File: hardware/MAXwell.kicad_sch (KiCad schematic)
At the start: 155 parts, among them J1 Conn_02x05_Odd_Even, J2 Conn_02x12_Counter_Clockwise, J3 Barrel_Jack_Switch_Pin3Ring, SW1 SW_Push_Dual, SW10 SW_Wuerth_450301014042, SW11 SW_Wuerth_450301014042, SW12 SW_Wuerth_450301014042, SW13 SW_Wuerth_450301014042, SW2 SW_Push_Dual, SW3 SW_Push_Dual, SW4 SW_Push_Dual, SW5 SW_Wuerth_450301014042, SW6 SW_Push_DPDT, SW7 SW_Wuerth_450301014042, SW8 SW_Wuerth_450301014042, SW9 SW_Wuerth_450301014042, U1 EPM240T100, U2 AMS1117-3.3, U3 D168K, U4 D168K, U5 D168K, U6 D168K, X1 50.000, X2 14.756

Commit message: all footprints assigned
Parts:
- C1: renamed from C11; footprint (none) -> Capacitor_SMD:C_0805_2012Metric_Pad1.18x1.45mm_HandSolder
- C10: renamed from C6; footprint (none) -> Capacitor_SMD:C_0805_2012Metric_Pad1.18x1.45mm_HandSolder
- C11: renamed from C7; footprint (none) -> Capacitor_SMD:C_0805_2012Metric_Pad1.18x1.45mm_HandSolder
- C12: renamed from C8; footprint (none) -> Capacitor_SMD:C_0805_2012Metric_Pad1.18x1.45mm_HandSolder
- C13: footprint (none) -> Capacitor_SMD:C_0805_2012Metric_Pad1.18x1.45mm_HandSolder
- C14: renamed from C15; footprint (none) -> Capacitor_SMD:C_0805_2012Metric_Pad1.18x1.45mm_HandSolder
- C15: renamed from C20; footprint (none) -> Capacitor_SMD:C_0805_2012Metric_Pad1.18x1.45mm_HandSolder
- C16: renamed from C25; footprint (none) -> Capacitor_SMD:C_0805_2012Metric_Pad1.18x1.45mm_HandSolder
- C17: renamed from C23; footprint (none) -> Capacitor_SMD:C_0805_2012Metric_Pad1.18x1.45mm_HandSolder
- C18: renamed from C19; footprint (none) -> Capacitor_SMD:C_0805_2012Metric_Pad1.18x1.45mm_HandSolder
- C19: renamed from C17; footprint (none) -> Capacitor_THT:CP_Radial_D5.0mm_P2.00mm; Part-Nr (none) -> M-A 100U 16-2
- C2: renamed from C12; footprint (none) -> Capacitor_SMD:C_0805_2012Metric_Pad1.18x1.45mm_HandSolder
- C20: renamed from C24; footprint (none) -> Capacitor_SMD:C_0805_2012Metric_Pad1.18x1.45mm_HandSolder
- C21: renamed from C22; footprint (none) -> Capacitor_SMD:C_0805_2012Metric_Pad1.18x1.45mm_HandSolder
- C22: renamed from C18; footprint (none) -> Capacitor_SMD:C_0805_2012Metric_Pad1.18x1.45mm_HandSolder
- C23: renamed from C21; footprint (none) -> Capacitor_SMD:C_0805_2012Metric_Pad1.18x1.45mm_HandSolder
- C24: renamed from C9; footprint (none) -> Capacitor_SMD:C_0805_2012Metric_Pad1.18x1.45mm_HandSolder
- C25: renamed from C10; footprint (none) -> Capacitor_SMD:C_0805_2012Metric_Pad1.18x1.45mm_HandSolder
- C3: renamed from C16; footprint (none) -> Capacitor_SMD:C_0805_2012Metric_Pad1.18x1.45mm_HandSolder
- C4: renamed from C1; footprint (none) -> Capacitor_SMD:C_0805_2012Metric_Pad1.18x1.45mm_HandSolder
- C5: renamed from C2; footprint (none) -> Capacitor_SMD:C_0805_2012Metric_Pad1.18x1.45mm_HandSolder
- C6: renamed from C3; footprint (none) -> Capacitor_SMD:C_0805_2012Metric_Pad1.18x1.45mm_HandSolder
- C7: renamed from C4; footprint (none) -> Capacitor_SMD:C_0805_2012Metric_Pad1.18x1.45mm_HandSolder
- C8: renamed from C5; footprint (none) -> Capacitor_SMD:C_0805_2012Metric_Pad1.18x1.45mm_HandSolder
- C9: renamed from C14; footprint (none) -> Capacitor_SMD:C_0805_2012Metric_Pad1.18x1.45mm_HandSolder
- D1: renamed from D5; footprint (none) -> LED_SMD:LED_0805_2012Metric_Pad1.15x1.40mm_HandSolder
- D10: renamed from D13; footprint (none) -> LED_SMD:LED_0805_2012Metric_Pad1.15x1.40mm_HandSolder
- D11: renamed from D14; footprint (none) -> LED_SMD:LED_0805_2012Metric_Pad1.15x1.40mm_HandSolder
- D12: renamed from D15; footprint (none) -> LED_SMD:LED_0805_2012Metric_Pad1.15x1.40mm_HandSolder
- D13: renamed from D16; footprint (none) -> LED_SMD:LED_0805_2012Metric_Pad1.15x1.40mm_HandSolder
- D14: renamed from D1; footprint (none) -> LED_SMD:LED_0805_2012Metric_Pad1.15x1.40mm_HandSolder
- D15: renamed from D2; footprint (none) -> LED_SMD:LED_0805_2012Metric_Pad1.15x1.40mm_HandSolder
- D16: renamed from D4; footprint (none) -> LED_SMD:LED_0805_2012Metric_Pad1.15x1.40mm_HandSolder
- D17: footprint (none) -> LED_SMD:LED_0805_2012Metric_Pad1.15x1.40mm_HandSolder
- D2: renamed from D6; footprint (none) -> LED_SMD:LED_0805_2012Metric_Pad1.15x1.40mm_HandSolder
- D3: renamed from D7; footprint (none) -> LED_SMD:LED_0805_2012Metric_Pad1.15x1.40mm_HandSolder
- D4: renamed from D8; footprint (none) -> LED_SMD:LED_0805_2012Metric_Pad1.15x1.40mm_HandSolder
- D5: renamed from D3; footprint (none) -> LED_SMD:LED_0805_2012Metric_Pad1.15x1.40mm_HandSolder
- D6: renamed from D9; footprint (none) -> LED_SMD:LED_0805_2012Metric_Pad1.15x1.40mm_HandSolder
- D7: renamed from D10; footprint (none) -> LED_SMD:LED_0805_2012Metric_Pad1.15x1.40mm_HandSolder
- D8: renamed from D11; footprint (none) -> LED_SMD:LED_0805_2012Metric_Pad1.15x1.40mm_HandSolder
- D9: renamed from D12; footprint (none) -> LED_SMD:LED_0805_2012Metric_Pad1.15x1.40mm_HandSolder
- J2: footprint (none) -> Connector_PinHeader_2.54mm:PinHeader_2x12_P2.54mm_Horizontal
- J3: footprint Connector_BarrelJack:BarrelJack_CUI_PJ-063AH_Horizontal_CircularHoles -> Connector_BarrelJack:BarrelJack_Horizontal
- R1: renamed from R5; footprint (none) -> Resistor_SMD:R_0805_2012Metric_Pad1.20x1.40mm_HandSolder
- R10: renamed from R37; footprint (none) -> Resistor_SMD:R_0805_2012Metric_Pad1.20x1.40mm_HandSolder
- R11: renamed from R38; footprint (none) -> Resistor_SMD:R_0805_2012Metric_Pad1.20x1.40mm_HandSolder
- R12: renamed from R39; footprint (none) -> Resistor_SMD:R_0805_2012Metric_Pad1.20x1.40mm_HandSolder
- R13: renamed from R40; footprint (none) -> Resistor_SMD:R_0805_2012Metric_Pad1.20x1.40mm_HandSolder
- R14: renamed from R25; footprint (none) -> Resistor_SMD:R_0805_2012Metric_Pad1.20x1.40mm_HandSolder
- R15: renamed from R26; footprint (none) -> Resistor_SMD:R_0805_2012Metric_Pad1.20x1.40mm_HandSolder
- R16: renamed from R27; footprint (none) -> Resistor_SMD:R_0805_2012Metric_Pad1.20x1.40mm_HandSolder
- R17: renamed from R28; footprint (none) -> Resistor_SMD:R_0805_2012Metric_Pad1.20x1.40mm_HandSolder
- R18: renamed from R29; footprint (none) -> Resistor_SMD:R_0805_2012Metric_Pad1.20x1.40mm_HandSolder
- R19: renamed from R30; footprint (none) -> Resistor_SMD:R_0805_2012Metric_Pad1.20x1.40mm_HandSolder
- R2: renamed from R6; footprint (none) -> Resistor_SMD:R_0805_2012Metric_Pad1.20x1.40mm_HandSolder
- R20: renamed from R31; footprint (none) -> Resistor_SMD:R_0805_2012Metric_Pad1.20x1.40mm_HandSolder
- R21: renamed from R32; footprint (none) -> Resistor_SMD:R_0805_2012Metric_Pad1.20x1.40mm_HandSolder
- R22: renamed from R41; footprint (none) -> Resistor_SMD:R_0805_2012Metric_Pad1.20x1.40mm_HandSolder
- R23: renamed from R42; footprint (none) -> Resistor_SMD:R_0805_2012Metric_Pad1.20x1.40mm_HandSolder
- R24: renamed from R43; footprint (none) -> Resistor_SMD:R_0805_2012Metric_Pad1.20x1.40mm_HandSolder
- R25: renamed from R44; footprint (none) -> Resistor_SMD:R_0805_2012Metric_Pad1.20x1.40mm_HandSolder
- R26: renamed from R45; footprint (none) -> Resistor_SMD:R_0805_2012Metric_Pad1.20x1.40mm_HandSolder
- R27: renamed from R46; footprint (none) -> Resistor_SMD:R_0805_2012Metric_Pad1.20x1.40mm_HandSolder
- R28: renamed from R47; footprint (none) -> Resistor_SMD:R_0805_2012Metric_Pad1.20x1.40mm_HandSolder
- R29: renamed from R48; footprint (none) -> Resistor_SMD:R_0805_2012Metric_Pad1.20x1.40mm_HandSolder
- R3: renamed from R7; footprint (none) -> Resistor_SMD:R_0805_2012Metric_Pad1.20x1.40mm_HandSolder
- R30: renamed from R64; footprint (none) -> Resistor_SMD:R_0805_2012Metric_Pad1.20x1.40mm_HandSolder
- R31: renamed from R63; footprint (none) -> Resistor_SMD:R_0805_2012Metric_Pad1.20x1.40mm_HandSolder
- R32: renamed from R62; footprint (none) -> Resistor_SMD:R_0805_2012Metric_Pad1.20x1.40mm_HandSolder
- R33: renamed from R61; footprint (none) -> Resistor_SMD:R_0805_2012Metric_Pad1.20x1.40mm_HandSolder
- R34: renamed from R17; footprint (none) -> Resistor_SMD:R_0805_2012Metric_Pad1.20x1.40mm_HandSolder
- R35: renamed from R18; footprint (none) -> Resistor_SMD:R_0805_2012Metric_Pad1.20x1.40mm_HandSolder
- R36: renamed from R19; footprint (none) -> Resistor_SMD:R_0805_2012Metric_Pad1.20x1.40mm_HandSolder
- R37: renamed from R20; footprint (none) -> Resistor_SMD:R_0805_2012Metric_Pad1.20x1.40mm_HandSolder
- R38: renamed from R21; footprint (none) -> Resistor_SMD:R_0805_2012Metric_Pad1.20x1.40mm_HandSolder
- R39: renamed from R22; footprint (none) -> Resistor_SMD:R_0805_2012Metric_Pad1.20x1.40mm_HandSolder
- R4: renamed from R8; footprint (none) -> Resistor_SMD:R_0805_2012Metric_Pad1.20x1.40mm_HandSolder
- R40: renamed from R23; footprint (none) -> Resistor_SMD:R_0805_2012Metric_Pad1.20x1.40mm_HandSolder
- R41: renamed from R24; footprint (none) -> Resistor_SMD:R_0805_2012Metric_Pad1.20x1.40mm_HandSolder
- R42: renamed from R58; footprint (none) -> Resistor_SMD:R_0805_2012Metric_Pad1.20x1.40mm_HandSolder
- R43: renamed from R59; footprint (none) -> Resistor_SMD:R_0805_2012Metric_Pad1.20x1.40mm_HandSolder
- R44: renamed from R60; footprint (none) -> Resistor_SMD:R_0805_2012Metric_Pad1.20x1.40mm_HandSolder
- R45: renamed from R52; footprint (none) -> Resistor_SMD:R_0805_2012Metric_Pad1.20x1.40mm_HandSolder
- R46: renamed from R53; footprint (none) -> Resistor_SMD:R_0805_2012Metric_Pad1.20x1.40mm_HandSolder
- R47: renamed from R54; footprint (none) -> Resistor_SMD:R_0805_2012Metric_Pad1.20x1.40mm_HandSolder
- R48: renamed from R49; footprint (none) -> Resistor_SMD:R_0805_2012Metric_Pad1.20x1.40mm_HandSolder
- R49: renamed from R50; footprint (none) -> Resistor_SMD:R_0805_2012Metric_Pad1.20x1.40mm_HandSolder
- R5: renamed from R3; footprint (none) -> Resistor_SMD:R_0805_2012Metric_Pad1.20x1.40mm_HandSolder
- R50: renamed from R55; footprint (none) -> Resistor_SMD:R_0805_2012Metric_Pad1.20x1.40mm_HandSolder
- R51: renamed from R56; footprint (none) -> Resistor_SMD:R_0805_2012Metric_Pad1.20x1.40mm_HandSolder
- R52: renamed from R9; footprint (none) -> Resistor_SMD:R_0805_2012Metric_Pad1.20x1.40mm_HandSolder
- R53: renamed from R10; footprint (none) -> Resistor_SMD:R_0805_2012Metric_Pad1.20x1.40mm_HandSolder
- R54: renamed from R11; footprint (none) -> Resistor_SMD:R_0805_2012Metric_Pad1.20x1.40mm_HandSolder
- R55: renamed from R12; footprint (none) -> Resistor_SMD:R_0805_2012Metric_Pad1.20x1.40mm_HandSolder
- R56: renamed from R13; footprint (none) -> Resistor_SMD:R_0805_2012Metric_Pad1.20x1.40mm_HandSolder
- R57: renamed from R14; footprint (none) -> Resistor_SMD:R_0805_2012Metric_Pad1.20x1.40mm_HandSolder
- R58: renamed from R15; footprint (none) -> Resistor_SMD:R_0805_2012Metric_Pad1.20x1.40mm_HandSolder
- R59: renamed from R16; footprint (none) -> Resistor_SMD:R_0805_2012Metric_Pad1.20x1.40mm_HandSolder
- R6: renamed from R33; footprint (none) -> Resistor_SMD:R_0805_2012Metric_Pad1.20x1.40mm_HandSolder
- R60: renamed from R51; footprint (none) -> Resistor_SMD:R_0805_2012Metric_Pad1.20x1.40mm_HandSolder
- R61: renamed from R57; footprint (none) -> Resistor_SMD:R_0805_2012Metric_Pad1.20x1.40mm_HandSolder
- R62: renamed from R1; footprint (none) -> Resistor_SMD:R_0805_2012Metric_Pad1.20x1.40mm_HandSolder
- R63: renamed from R2; footprint (none) -> Resistor_SMD:R_0805_2012Metric_Pad1.20x1.40mm_HandSolder
- R64: renamed from R72; footprint (none) -> Resistor_SMD:R_0805_2012Metric_Pad1.20x1.40mm_HandSolder
- R65: renamed from R4; footprint (none) -> Resistor_SMD:R_0805_2012Metric_Pad1.20x1.40mm_HandSolder
- R66: renamed from R73; footprint (none) -> Resistor_SMD:R_0805_2012Metric_Pad1.20x1.40mm_HandSolder
- R67: renamed from R74; footprint (none) -> Resistor_SMD:R_0805_2012Metric_Pad1.20x1.40mm_HandSolder
- R68: renamed from R87; footprint (none) -> Resistor_SMD:R_0805_2012Metric_Pad1.20x1.40mm_HandSolder
- R69: renamed from R81; footprint (none) -> Resistor_SMD:R_0805_2012Metric_Pad1.20x1.40mm_HandSolder
- R7: renamed from R34; footprint (none) -> Resistor_SMD:R_0805_2012Metric_Pad1.20x1.40mm_HandSolder
- R70: renamed from R69; footprint (none) -> Resistor_SMD:R_0805_2012Metric_Pad1.20x1.40mm_HandSolder
- R71: renamed from R88; footprint (none) -> Resistor_SMD:R_0805_2012Metric_Pad1.20x1.40mm_HandSolder
- R72: renamed from R89; footprint (none) -> Resistor_SMD:R_0805_2012Metric_Pad1.20x1.40mm_HandSolder
- R73: renamed from R82; footprint (none) -> Resistor_SMD:R_0805_2012Metric_Pad1.20x1.40mm_HandSolder
- R74: renamed from R83; footprint (none) -> Resistor_SMD:R_0805_2012Metric_Pad1.20x1.40mm_HandSolder
- R75: renamed from R70; footprint (none) -> Resistor_SMD:R_0805_2012Metric_Pad1.20x1.40mm_HandSolder
- R76: renamed from R71; footprint (none) -> Resistor_SMD:R_0805_2012Metric_Pad1.20x1.40mm_HandSolder
- R77: renamed from R65; footprint (none) -> Resistor_SMD:R_0805_2012Metric_Pad1.20x1.40mm_HandSolder
- R78: renamed from R84; footprint (none) -> Resistor_SMD:R_0805_2012Metric_Pad1.20x1.40mm_HandSolder
- R79: renamed from R78; footprint (none) -> Resistor_SMD:R_0805_2012Metric_Pad1.20x1.40mm_HandSolder
- R8: renamed from R35; footprint (none) -> Resistor_SMD:R_0805_2012Metric_Pad1.20x1.40mm_HandSolder
- R80: renamed from R68; footprint (none) -> Resistor_SMD:R_0805_2012Metric_Pad1.20x1.40mm_HandSolder
- R81: renamed from R75; footprint (none) -> Resistor_SMD:R_0805_2012Metric_Pad1.20x1.40mm_HandSolder
- R82: renamed from R85; footprint (none) -> Resistor_SMD:R_0805_2012Metric_Pad1.20x1.40mm_HandSolder
- R83: renamed from R86; footprint (none) -> Resistor_SMD:R_0805_2012Metric_Pad1.20x1.40mm_HandSolder
- R84: renamed from R79; footprint (none) -> Resistor_SMD:R_0805_2012Metric_Pad1.20x1.40mm_HandSolder
- R85: renamed from R80; footprint (none) -> Resistor_SMD:R_0805_2012Metric_Pad1.20x1.40mm_HandSolder
- R86: renamed from R67; footprint (none) -> Resistor_SMD:R_0805_2012Metric_Pad1.20x1.40mm_HandSolder
- R87: renamed from R66; footprint (none) -> Resistor_SMD:R_0805_2012Metric_Pad1.20x1.40mm_HandSolder
- R88: renamed from R76; footprint (none) -> Resistor_SMD:R_0805_2012Metric_Pad1.20x1.40mm_HandSolder
- R89: renamed from R77; footprint (none) -> Resistor_SMD:R_0805_2012Metric_Pad1.20x1.40mm_HandSolder
- R9: renamed from R36; footprint (none) -> Resistor_SMD:R_0805_2012Metric_Pad1.20x1.40mm_HandSolder
- SW10: renamed from SW12; footprint Button_Switch_THT:SW_Slide-03_Wuerth-WS-SLTV_10x2.5x6.4_P2.54mm -> Library:SW_Slide_SPDT_Straight_12.8mm_6.9mm
- SW11: renamed from SW10; footprint Button_Switch_THT:SW_Slide-03_Wuerth-WS-SLTV_10x2.5x6.4_P2.54mm -> Library:SW_Slide_SPDT_Straight_12.8mm_6.9mm
- SW12: renamed from SW5; footprint Button_Switch_THT:SW_Slide-03_Wuerth-WS-SLTV_10x2.5x6.4_P2.54mm -> Library:SW_Slide_SPDT_Straight_12.8mm_6.9mm
- SW13: renamed from SW9; footprint Button_Switch_THT:SW_Slide-03_Wuerth-WS-SLTV_10x2.5x6.4_P2.54mm -> Library:SW_Slide_SPDT_Straight_12.8mm_6.9mm
- SW5: renamed from SW8; footprint Button_Switch_THT:SW_Slide-03_Wuerth-WS-SLTV_10x2.5x6.4_P2.54mm -> Library:SW_Slide_SPDT_Straight_12.8mm_6.9mm
- SW6: renamed from SW13; footprint Button_Switch_THT:SW_Slide-03_Wuerth-WS-SLTV_10x2.5x6.4_P2.54mm -> Library:SW_Slide_SPDT_Straight_12.8mm_6.9mm
- SW7: renamed from SW11; footprint Button_Switch_THT:SW_Slide-03_Wuerth-WS-SLTV_10x2.5x6.4_P2.54mm -> Library:SW_Slide_SPDT_Straight_12.8mm_6.9mm
- SW8: renamed from SW7; footprint Button_Switch_THT:SW_Slide-03_Wuerth-WS-SLTV_10x2.5x6.4_P2.54mm -> Library:SW_Slide_SPDT_Straight_12.8mm_6.9mm
- SW9: renamed from SW6; footprint (none) -> Button_Switch_THT:SW_Push_2P2T_Toggle_CK_PVA2OAH5xxxxxxV2
- U1: renamed from U5; Part-Nr SA 56-11 RT Alternative: SC 39-11 GN -> SA 56-11 RT
- renumbered SW4 to SW1, SW1 to SW3, SW3 to SW4, U4 to U2, U6 to U3, U3 to U4, U1 to U5, U2 to U6
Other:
- note added: "TODO: Prüfen, ob Prog. Header richtig angeschlossen Pin 10 mit GND Verbidung richtig?"
- note removed: "TODO: Prüfen, ob Prog. Header richtig angeschlossen"

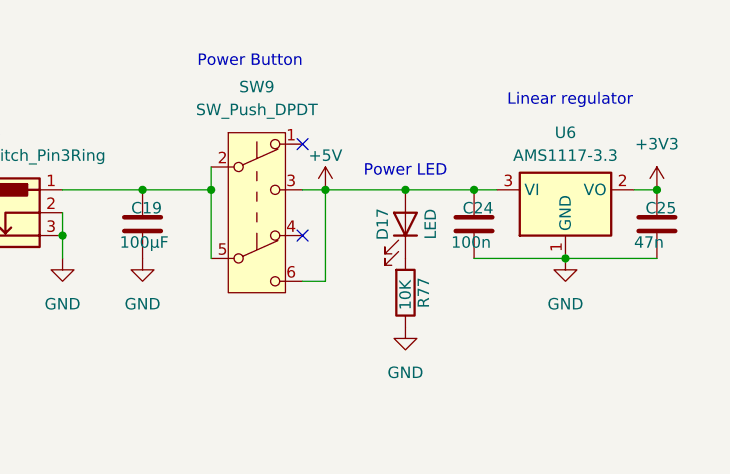
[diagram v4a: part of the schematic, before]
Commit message: ERC applied and fixed missing power flags
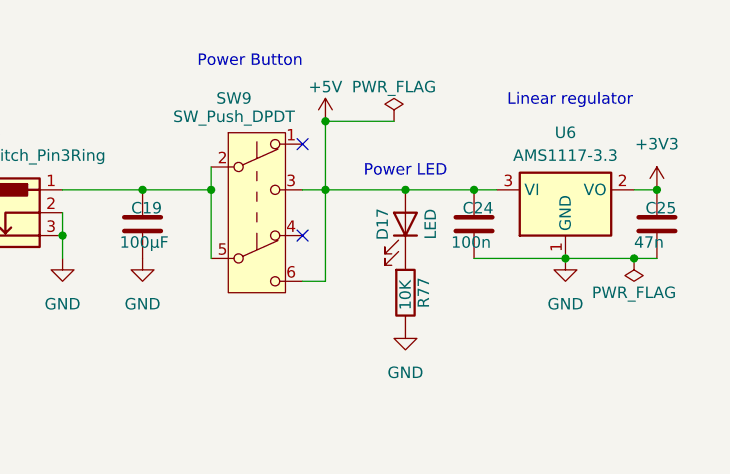
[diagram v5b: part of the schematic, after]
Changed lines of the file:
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@@
 	)
 	(junction
+		(at 274.32 39.37)
+		(diameter 0)
+		(color 0 0 0 0)
+	)
+	(junction
 		(at 31.75 34.29)
 		(diameter 0)
@@
 	)
 	(junction
+		(at 240.03 24.13)
+		(diameter 0)
+		(color 0 0 0 0)
+	)
+	(junction
 		(at 64.77 111.76)
 		(diameter 0)
@@
 	(wire
 		(pts
+			(xy 274.32 39.37) (xy 276.86 39.37)
+		)
+		(stroke
+			(width 0)
+			(type default)
+		)
+	)
+	(wire
+		(pts
 			(xy 181.61 29.21) (xy 181.61 35.56)
 		)
@@
 	(wire
 		(pts
+			(xy 247.65 24.13) (xy 240.03 24.13)
+		)
+		(stroke
+			(width 0)
+			(type default)
+		)
+	)
+	(wire
+		(pts
 			(xy 142.24 83.82) (xy 146.05 83.82)
 		)
@@
 	(wire
 		(pts
+			(xy 240.03 24.13) (xy 240.03 31.75)
+		)
+		(stroke
+			(width 0)
+			(type default)
+		)
+	)
+	(wire
+		(pts
 			(xy 60.96 116.84) (xy 91.44 116.84)
 		)
@@
 	(wire
 		(pts
-			(xy 266.7 39.37) (xy 276.86 39.37)
+			(xy 266.7 39.37) (xy 274.32 39.37)
 		)
 		(stroke
@@
 	(symbol
 		(lib_id "power:+5V")
-		(at 240.03 31.75 0)
+		(at 240.03 24.13 0)
 		(unit 1)
 		(exclude_from_sim no)
@@
 		(dnp no)
 		(property "Reference" "#PWR043"
-			(at 240.03 35.56 0)
+			(at 240.03 27.94 0)
 			(effects
 				(font
@@
 		)
 		(property "Value" "+5V"
-			(at 240.03 27.94 0)
+			(at 240.03 20.32 0)
 			(effects
 				(font
@@
 		)
 		(property "Footprint" ""
-			(at 240.03 31.75 0)
+			(at 240.03 24.13 0)
 			(effects
 				(font
@@
 		)
 		(property "Datasheet" ""
-			(at 240.03 31.75 0)
+			(at 240.03 24.13 0)
 			(effects
 				(font
@@
 		)
 		(property "Description" "Power symbol creates a global label with name \"+5V\""
-			(at 240.03 31.75 0)
+			(at 240.03 24.13 0)
 			(effects
 				(font
@@
 		(on_board yes)
 		(dnp no)
-		(fields_autoplaced yes)
 		(property "Reference" "SW9"
-			(at 232.41 20.32 0)
+			(at 229.87 21.59 0)
 			(effects
 				(font
@@
 		)
 		(property "Value" "SW_Push_DPDT"
-			(at 232.41 22.86 0)
+			(at 229.87 23.622 0)
 			(effects
 				(font
@@
 	)
 	(symbol
+		(lib_id "power:PWR_FLAG")
+		(at 274.32 39.37 180)
+		(unit 1)
+		(exclude_from_sim no)
+		(in_bom yes)
+		(on_board yes)
+		(dnp no)
+		(property "Reference" "#FLG02"
+			(at 274.32 41.275 0)
+			(effects
+				(font
+					(size 1.27 1.27)
+				)
+				(hide yes)
+			)
+		)
+		(property "Value" "PWR_FLAG"
+			(at 274.32 43.18 0)
+			(effects
+				(font
+					(size 1.27 1.27)
+				)
+			)
+		)
+		(property "Footprint" ""
+			(at 274.32 39.37 0)
+			(effects
+				(font
+					(size 1.27 1.27)
+				)
+				(hide yes)
+			)
+		)
+		(property "Datasheet" "~"
+			(at 274.32 39.37 0)
+			(effects
+				(font
+					(size 1.27 1.27)
+				)
+				(hide yes)
+			)
+		)
+		(property "Description" "Special symbol for telling ERC where power comes from"
+			(at 274.32 39.37 0)
+			(effects
+				(font
+					(size 1.27 1.27)
+				)
+				(hide yes)
+			)
+		)
+		(pin "1"
+		)
+		(instances
+			(project "MAXwell"
+				(path "/fb6af602-47f1-4d32-af46-a424ef1eeea7"
+					(reference "#FLG02")
+					(unit 1)
+				)
+			)
+		)
+	)
+	(symbol
 		(lib_id "power:+3V3")
 		(at 31.75 19.05 0)
@@
 					(unit 1)
 				)
+			)
+		)
+	)
+	(symbol
+		(lib_id "power:PWR_FLAG")
+		(at 247.65 24.13 0)
+		(unit 1)
+		(exclude_from_sim no)
+		(in_bom yes)
+		(on_board yes)
+		(dnp no)
+		(property "Reference" "#FLG01"
+			(at 247.65 22.225 0)
+			(effects
+				(font
+					(size 1.27 1.27)
+				)
+				(hide yes)
+			)
+		)
+		(property "Value" "PWR_FLAG"
+			(at 247.65 20.32 0)
+			(effects
+				(font
+					(size 1.27 1.27)
+				)
+			)
+		)
+		(property "Footprint" ""
+			(at 247.65 24.13 0)
+			(effects
+				(font
+					(size 1.27 1.27)
+				)
+				(hide yes)
+			)
+		)
+		(property "Datasheet" "~"
+			(at 247.65 24.13 0)
+			(effects
+				(font
+					(size 1.27 1.27)
+				)
+				(hide yes)
+			)
+		)
+		(property "Description" "Special symbol for telling ERC where power comes from"
+			(at 247.65 24.13 0)
+			(effects
+				(font
+					(size 1.27 1.27)
+				)
+				(hide yes)
+			)
+		)
+		(pin "1"
+		)
+		(instances
+			(project "MAXwell"
+				(path "/fb6af602-47f1-4d32-af46-a424ef1eeea7"
+					(reference "#FLG01")
+					(unit 1)
+				)

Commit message: started routing
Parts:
- J2: symbol Connector_Generic:Conn_02x12_Counter_Clockwise -> Connector_Generic:Conn_02x12_Odd_Even
- SW1, SW2, SW3, SW4: footprint Button_Switch_THT:SW_PUSH-12mm -> Library:SW_PUSH-12mm
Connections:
- net +3V3: now also J2.3 (Pin_3); no longer J2.2 (Pin_2)
- net GND: now also J2.2 (Pin_2), J2.4 (Pin_4), J2.6 (Pin_6), J2.8 (Pin_8); no longer J2.21 (Pin_21), J2.22 (Pin_22), J2.23 (Pin_23), J2.24 (Pin_24)
- net at U5.62 (IO2_62/GCLK2): now also J2.5 (Pin_5); no longer J2.3 (Pin_3)
- net at U5.64 (IO2_64/GCLK3): now also J2.7 (Pin_7); no longer J2.4 (Pin_4)
- net at U5.66 (IO2_66): now also J2.9 (Pin_9); no longer J2.5 (Pin_5)
- net at U5.67 (IO2_67): now also J2.11 (Pin_11); no longer J2.6 (Pin_6)
- net at U5.68 (IO2_68): now also J2.13 (Pin_13); no longer J2.7 (Pin_7)
- net at U5.69 (IO2_69): now also J2.15 (Pin_15); no longer J2.8 (Pin_8)
- net at U5.70 (IO2_70): now also J2.17 (Pin_17); no longer J2.9 (Pin_9)
- net at U5.71 (IO2_71): now also J2.19 (Pin_19); no longer J2.10 (Pin_10)
- net at U5.72 (IO2_72): now also J2.21 (Pin_21); no longer J2.11 (Pin_11)
- net at U5.73 (IO2_73): now also J2.23 (Pin_23); no longer J2.12 (Pin_12)
- net at U5.74 (IO2_74): now also J2.24 (Pin_24); no longer J2.13 (Pin_13)
- net at U5.75 (IO2_75): now also J2.22 (Pin_22); no longer J2.14 (Pin_14)
- net at U5.76 (IO2_76): now also J2.20 (Pin_20); no longer J2.15 (Pin_15)
- net at U5.77 (IO2_77): now also J2.18 (Pin_18); no longer J2.16 (Pin_16)
- net at U5.78 (IO2_78): now also J2.16 (Pin_16); no longer J2.17 (Pin_17)
- net at U5.81 (IO2_81): now also J2.14 (Pin_14); no longer J2.18 (Pin_18)
- net at U5.82 (IO2_82): now also J2.12 (Pin_12); no longer J2.19 (Pin_19)
- net at U5.83 (IO2_83): now also J2.10 (Pin_10); no longer J2.20 (Pin_20)
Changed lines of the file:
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@@
 	)
 	(symbol
-		(lib_id "Connector_Generic:Conn_02x12_Counter_Clockwise")
+		(lib_id "Connector_Generic:Conn_02x12_Odd_Even")
 		(at 171.45 91.44 270)
 		(unit 1)
@@
 			)
 		)
-		(property "Description" "Generic connector, double row, 02x12, counter clockwise pin numbering scheme (similar to DIP package numbering), script generated (kicad-library-utils/schlib/autogen/connector/)"
+		(property "Description" "Generic connector, double row, 02x12, odd/even pin numbering scheme (row 1 odd numbers, row 2 even numbers), script generated (kicad-library-utils/schlib/autogen/connector/)"
 			(at 171.45 91.44 0)
 			(effects
@@
 			)
 		)
-		(property "Footprint" "Button_Switch_THT:SW_PUSH-12mm"
+		(property "Footprint" "Library:SW_PUSH-12mm"
 			(at 163.83 177.8 0)
 			(effects
@@
 			)
 		)
-		(property "Footprint" "Button_Switch_THT:SW_PUSH-12mm"
+		(property "Footprint" "Library:SW_PUSH-12mm"
 			(at 101.6 177.8 0)
 			(effects
@@
 			)
 		)
-		(property "Footprint" "Button_Switch_THT:SW_PUSH-12mm"
+		(property "Footprint" "Library:SW_PUSH-12mm"
 			(at 132.08 179.07 0)
 			(effects
@@
 			)
 		)
-		(property "Footprint" "Button_Switch_THT:SW_PUSH-12mm"
+		(property "Footprint" "Library:SW_PUSH-12mm"
 			(at 165.1 157.48 0)
 			(effects

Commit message: fixed wrong part number
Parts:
- U2: Part-Nr SA 56-11 RT Alternative: SC 39-11 GN -> SA 56-11 RT
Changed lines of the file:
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@@
 			)
 		)
-		(property "Part-Nr" "SA 56-11 RT Alternative: SC 39-11 GN"
+		(property "Part-Nr" "SA 56-11 RT"
 			(at 44.45 81.28 0)
 			(effects
